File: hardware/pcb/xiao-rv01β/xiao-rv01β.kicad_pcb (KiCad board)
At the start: 2 copper layers, 21 parts, among them Q1 P-Ch -12V/-6A, Q2 P-Ch -12V/-6A, U1 XIAO ESP32C6, U2 ADS1015, U3 ADS1015, U5 MCP23017

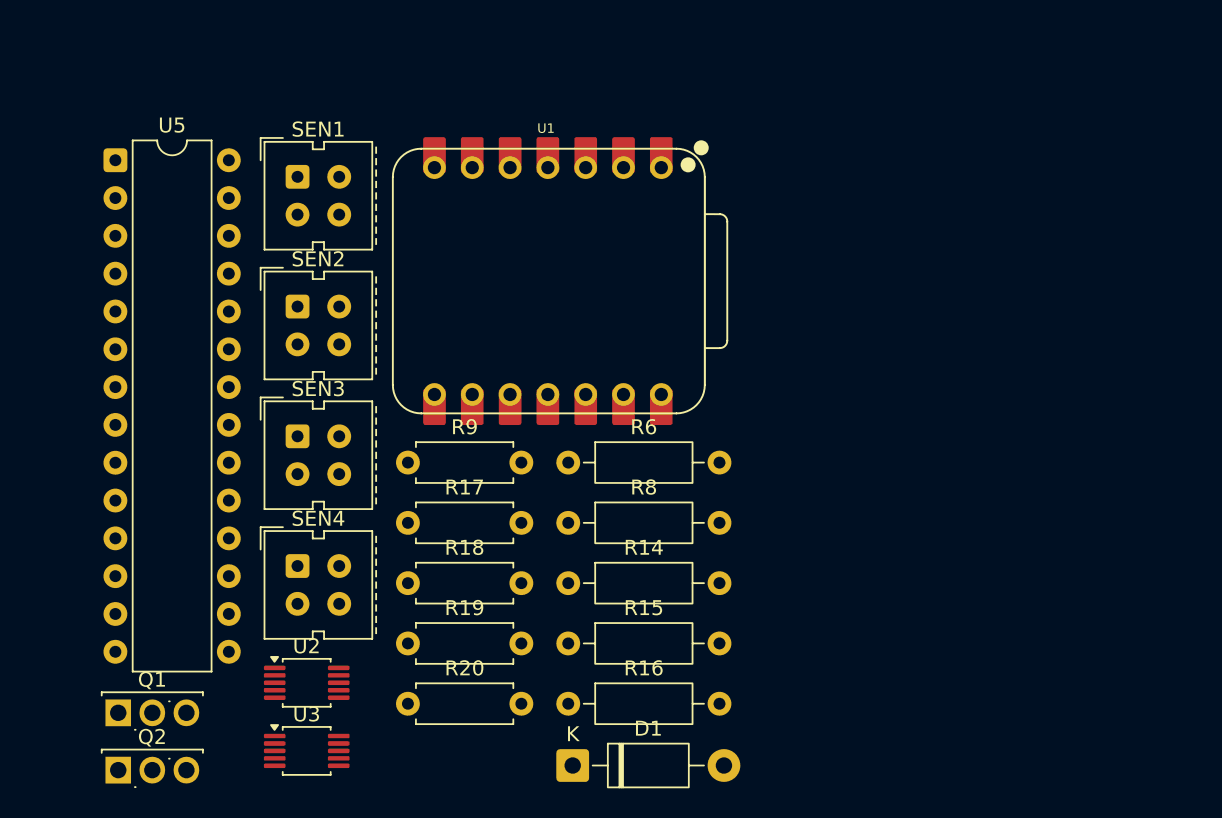
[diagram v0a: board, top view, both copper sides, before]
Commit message: switched to xiao esp32s3 plus & SPI-based expansion
Signed-off-by: Takuto Nagami <logica0419@gmail.com>
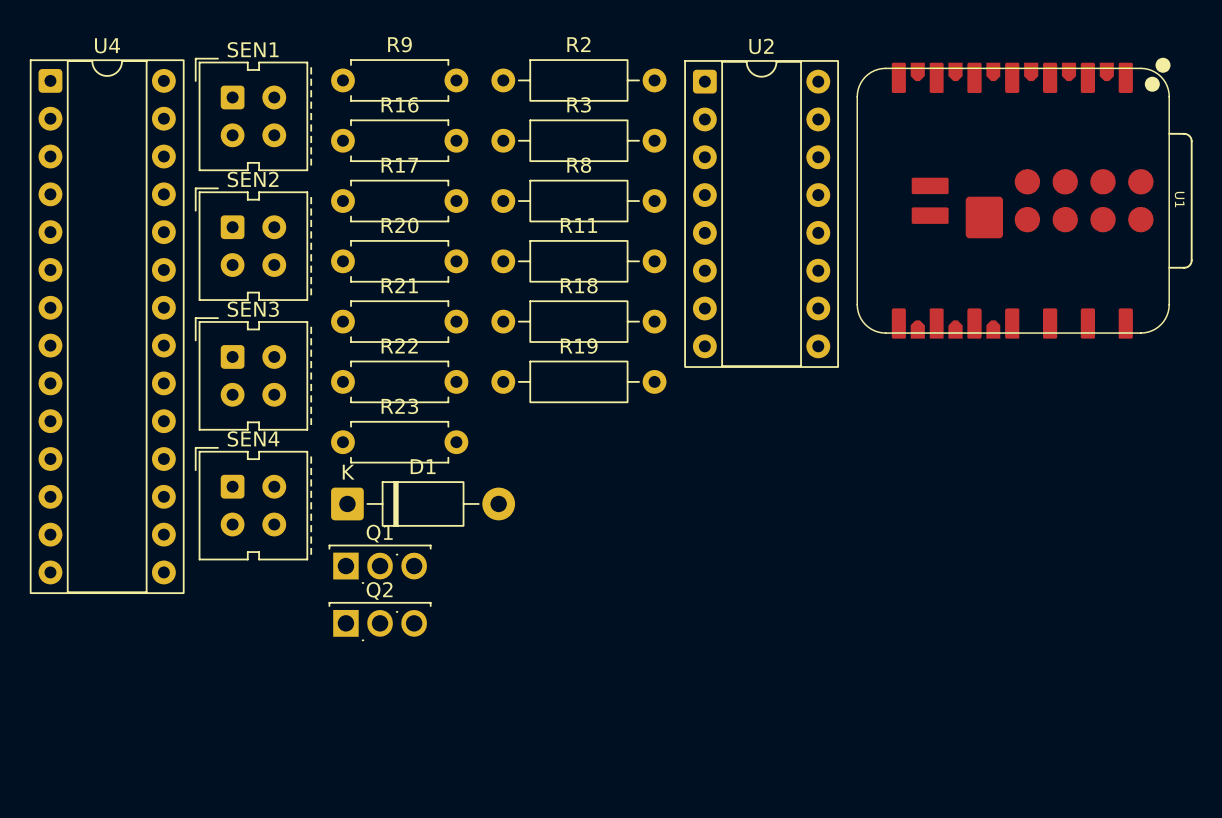
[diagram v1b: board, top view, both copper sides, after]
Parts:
- removed R14, R6: 22kΩ, Resistor_THT:R_Axial_DIN0207_L6.3mm_D2.5mm_P10.16mm_Horizontal
- removed R15: 100kΩ, Resistor_THT:R_Axial_DIN0207_L6.3mm_D2.5mm_P10.16mm_Horizontal
- removed U3: ADS1015, Package_SO:TSSOP-10_3x3mm_P0.5mm
- removed U5: MCP23017, Package_DIP:DIP-28_W7.62mm
- added R11: 22kΩ, Resistor_THT:R_Axial_DIN0207_L6.3mm_D2.5mm_P10.16mm_Horizontal, F.Cu at (47.0, 28.7)
- added R2: 100kΩ, Resistor_THT:R_Axial_DIN0207_L6.3mm_D2.5mm_P10.16mm_Horizontal, F.Cu at (47.0, 16.5)
- added R21: 1kΩ, Resistor_THT:R_Axial_DIN0207_L6.3mm_D2.5mm_P7.62mm_Horizontal, F.Cu at (36.2, 32.7)
- added R22: 1kΩ, Resistor_THT:R_Axial_DIN0207_L6.3mm_D2.5mm_P7.62mm_Horizontal, F.Cu at (36.2, 36.8)
- added R23: 2.2kΩ, Resistor_THT:R_Axial_DIN0207_L6.3mm_D2.5mm_P7.62mm_Horizontal, F.Cu at (36.2, 40.8)
- added R3: 22kΩ, Resistor_THT:R_Axial_DIN0207_L6.3mm_D2.5mm_P10.16mm_Horizontal, F.Cu at (47.0, 20.6)
- added U4: MCP23S17, Package_DIP:DIP-28_W7.62mm_Socket, F.Cu at (16.6, 16.6)
- R16: value 33kΩ -> 2.2kΩ; footprint Resistor_THT:R_Axial_DIN0207_L6.3mm_D2.5mm_P10.16mm_Horizontal -> Resistor_THT:R_Axial_DIN0207_L6.3mm_D2.5mm_P7.62mm_Horizontal
- R18: value 1kΩ -> 33kΩ; footprint Resistor_THT:R_Axial_DIN0207_L6.3mm_D2.5mm_P7.62mm_Horizontal -> Resistor_THT:R_Axial_DIN0207_L6.3mm_D2.5mm_P10.16mm_Horizontal
- R19: value 1kΩ -> 100kΩ; footprint Resistor_THT:R_Axial_DIN0207_L6.3mm_D2.5mm_P7.62mm_Horizontal -> Resistor_THT:R_Axial_DIN0207_L6.3mm_D2.5mm_P10.16mm_Horizontal
- R8: value 100kΩ -> 22kΩ
- U1: value XIAO ESP32C6 -> XIAO-ESP32-S3-Plus; footprint New_XIAO_Series_Footprints:XIAO-ESP32-C6-DIP -> New_XIAO_Series_Footprints:XIAO-ESP32-S3-Plus-SMD
- U2: value ADS1015 -> MCP3208; footprint Package_SO:TSSOP-10_3x3mm_P0.5mm -> Package_DIP:DIP-16_W7.62mm_Socket
- moved U2 48.4 mm to (60.5, 16.6)
- moved R16 40.7 mm to (36.2, 20.6)
- moved U1 31.7 mm to (81.2, 24.6)
- moved R20 30.0 mm to (36.2, 28.7)
- moved R9 26.0 mm to (36.2, 16.5)
- moved D1 23.2 mm to (36.5, 45.0)
- moved R17 22.1 mm to (36.2, 24.6)
- moved R8 22.1 mm to (47.0, 24.6)
- moved R19 18.7 mm to (47.0, 36.8)
- moved R18 18.7 mm to (47.0, 32.7)
- moved Q2 18.2 mm to (36.4, 53.0)
- moved Q1 18.2 mm to (36.4, 49.1)
- moved SEN3 6.89 mm to (28.8, 35.1)
- moved SEN4 6.89 mm to (28.8, 43.8)
- moved SEN1 6.89 mm to (28.8, 17.7)
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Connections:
- net EXT3_PWM renamed EXT3_ADC/PWM
- R16 pad 1: Net-(U1-GPIO19_D8_SCK) -> 3V3
- R16 pad 2: GND -> SCL
- R17 pad 2: SCL -> IOE_CS
- R18 pad 1: Net-(BZ1-+) -> Net-(U1-GPIO11_DVP_Y8_SPI_MOSI1)
- R18 pad 2: BUZZER -> GND
- R19 pad 1: GND -> Net-(Q2-S)
- R19 pad 2: Net-(LED5-K) -> Net-(Q2-G)
- R20 pad 1: GND -> 3V3
- R20 pad 2: Net-(LED6-K) -> ADC_CS
- R8 pad 1: Net-(Q1-G) -> Net-(R10-Pad1)
- R8 pad 2: GND -> Net-(U1-GPIO1_A0_D0)
- U1 pad 1: Net-(U1-GPIO0_A0_D0) -> Net-(U1-GPIO1_A0_D0)
- U1 pad 10: MD_BENBL -> MISO
- U1 pad 11: MD_AENBL -> MOSI
- U1 pad 5: SDA -> EXT4_ADC/PWM
- U1 pad 6: SCL -> EXT5_ADC/PWM
- U1 pad 9: Net-(U1-GPIO19_D8_SCK) -> SCK
- U2 pad 1: 3V3 -> Net-(SEN4-E)
- U2 pad 10: SCL -> ADC_CS
- U2 pad 2: unconnected-(U2-ALERT/RDY-Pad2) -> Net-(SEN3-E)
- U2 pad 3: GND -> Net-(SEN2-E)
- U2 pad 4: Net-(SEN4-E) -> Net-(SEN1-E)
- U2 pad 5: Net-(SEN3-E) -> EXT6_ADC
- U2 pad 6: Net-(SEN2-E) -> EXT7_ADC
- U2 pad 7: Net-(SEN1-E) -> EXT8_ADC
- U2 pad 8: 3V3 -> EXT9_ADC
- U2 pad 9: SDA -> GND
